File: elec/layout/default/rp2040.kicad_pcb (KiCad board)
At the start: 2 copper layers, 20 parts

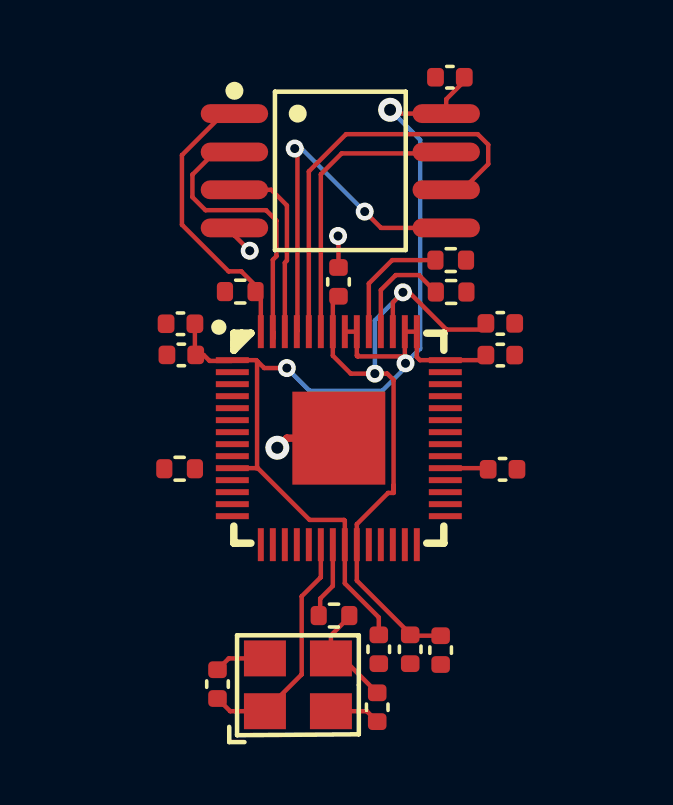
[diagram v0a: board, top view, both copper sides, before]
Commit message: Update layout to v0.3 compiler
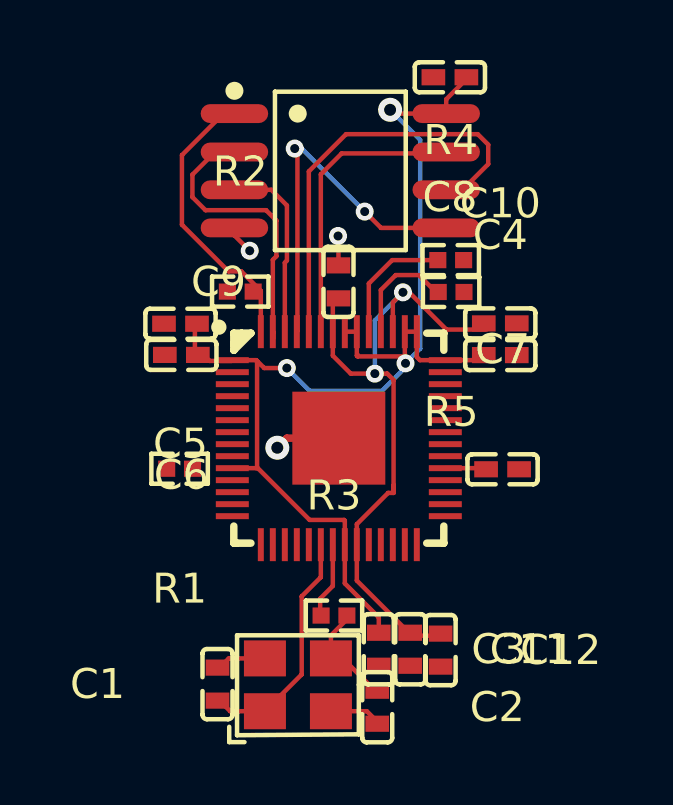
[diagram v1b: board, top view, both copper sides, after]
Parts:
- C1, C2: value 50V 20pF C0G ±5% 0402 Multilayer Ceramic Capacitors MLCC - SMD/SMT ROHS -> 20pF ±5% 50V C0G; footprint lib:C0402 -> lcsc:C0402
- C10, C11, C3, C4, C5, C6, C7, C9: value 16V 100nF X7R ±10% 0402 Multilayer Ceramic Capacitors MLCC - SMD/SMT ROHS -> 100nF ±10% 16V X7R; footprint lib:C0402 -> lcsc:C0402
- C12, C8: value 25V 1uF X5R ±10% 0402 Multilayer Ceramic Capacitors MLCC - SMD/SMT ROHS -> 1µF ±10% 16V X5R; footprint lib:C0402 -> lcsc:C0402
- R1, R2: value 62.5mW Thick Film Resistors ±100ppm/℃ ±1% 10kΩ 0402 Chip Resistor - Surface Mount ROHS -> 10kΩ ±1% 62.5mW; footprint lib:R0402 -> lcsc:R0402
- R3: value 62.5mW Thick Film Resistors ±100ppm/℃ ±1% 1kΩ 0402 Chip Resistor - Surface Mount ROHS -> 1kΩ ±1% 62.5mW; footprint lib:R0402 -> lcsc:R0402
- R4, R5: value 62.5mW Thick Film Resistors ±100ppm/℃ ±1% 27Ω 0402 Chip Resistor - Surface Mount ROHS -> 27Ω ±1% 62.5mW; footprint lib:R0402 -> lcsc:R0402
- U1: value (none) -> RP2040
- U2: value (none) -> _X322512MSB4SI
- U3: value (none) -> _W25Q128JVSIQ
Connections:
- net micro-vcc renamed hv-1
- net vcc renamed hv
- net xin renamed input
- C2 pad 1: out -> osc-out
- R1 pad 2: run -> out
- R2 pad 2: cs-1 -> cs
- R3 pad 2: out -> osc-out
- U1 pad 12: cs -> cs-1
- U1 pad 26: run -> out
- U1 pad 56: cs-1 -> cs
- U2 pad 3: out -> osc-out
- U3 pad 1: cs-1 -> cs
